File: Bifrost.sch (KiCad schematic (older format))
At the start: 55 parts, among them J1 OIP, U3 LMH6881, X1 SPXO-50M

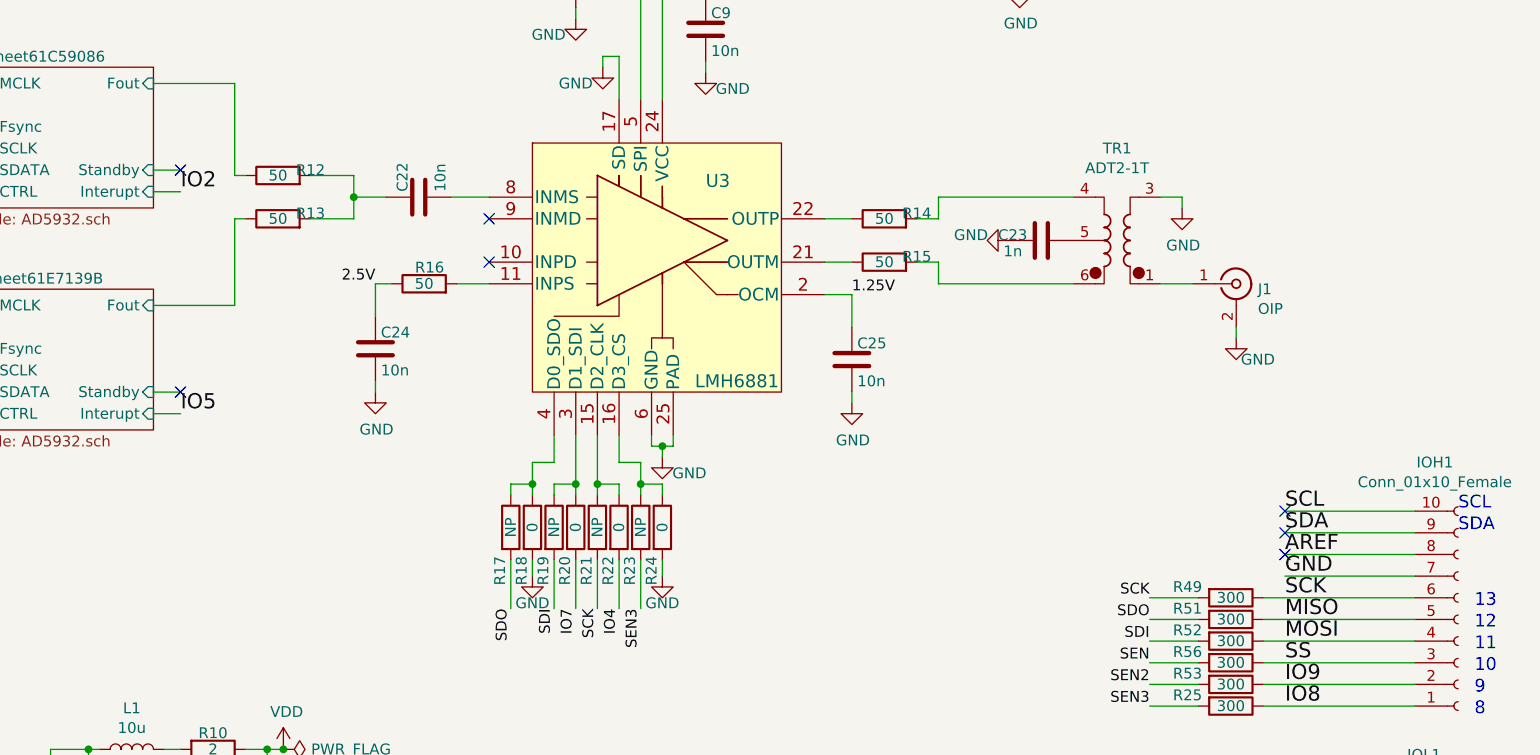
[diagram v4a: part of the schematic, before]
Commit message: put the AD5932's Standby to the ground
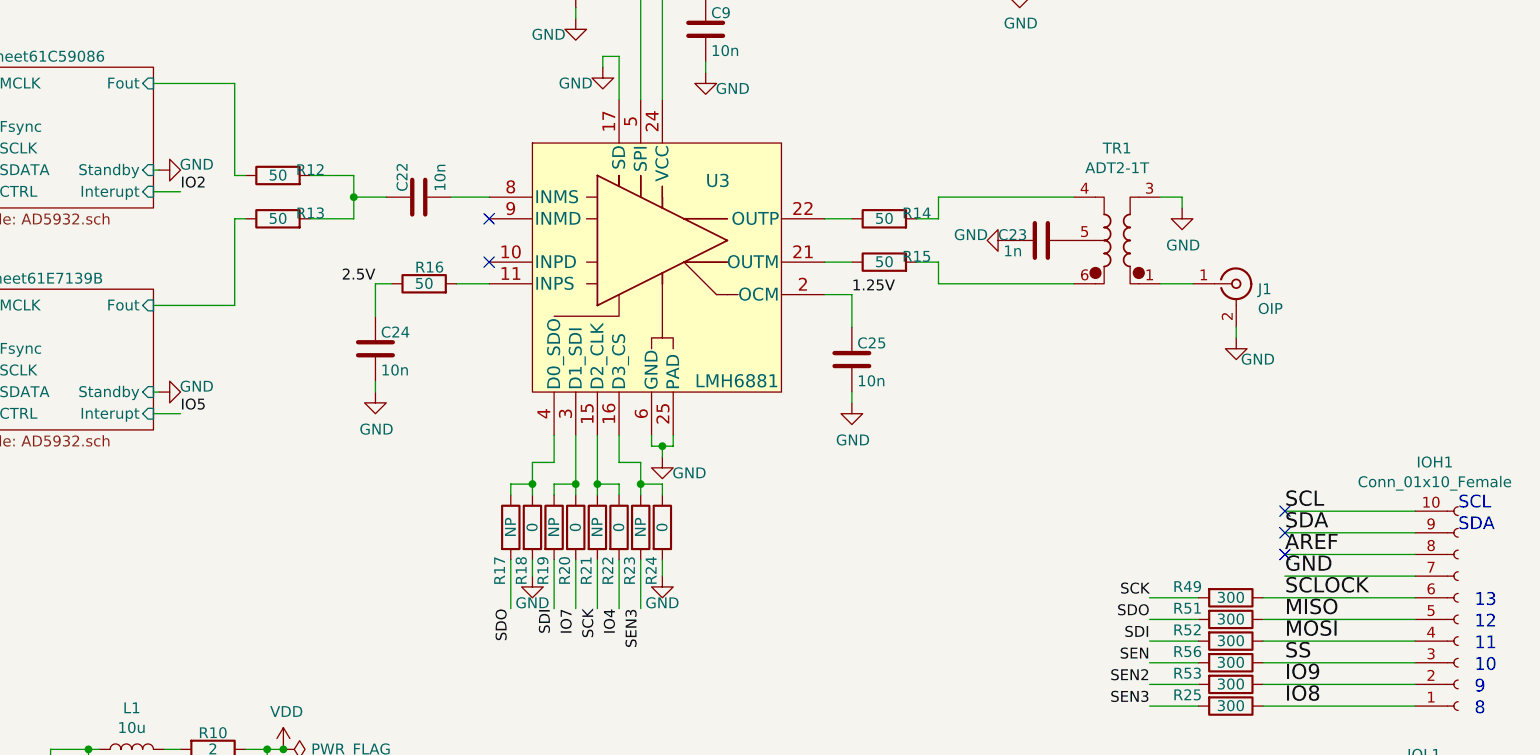
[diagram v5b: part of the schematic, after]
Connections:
- net SCK: no longer IOH1.6 (Pin_6), R49.1
- new net SCLOCK: IOH1.6 (Pin_6), R49.1
- no-connect marks 28 -> 26
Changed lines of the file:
@@
 GND
 Text Label 10000 4550 0    70   ~ 0
-SCK
+SCLOCK
 Text Label 10000 4650 0    70   ~ 0
 MISO
@@
 Text Label 3625 2675 2    70   ~ 0
 IO3
-Text Label 4900 2675 0    70   ~ 0
+Text Label 4900 2675 0    50   ~ 0
 IO2
 Wire Wire Line
@@
 	4775 2675 4900 2675
 Wire Wire Line
-	4775 2575 4900 2575
-Text Label 4900 3700 0    70   ~ 0
+	4775 2575 4800 2575
+Text Label 4900 3700 0    50   ~ 0
 IO5
 Text Label 3625 3700 2    70   ~ 0
@@
 	4775 3700 4900 3700
 Wire Wire Line
-	4775 3600 4900 3600
+	4775 3600 4800 3600
 Text Label 3625 3500 2    50   ~ 0
 SCK
@@
 Text Label 6725 4600 3    50   ~ 0
 IO7
-NoConn ~ 4900 3600
-NoConn ~ 4900 2575
 Wire Wire Line
 	6525 4375 6525 4450
@@
 Wire Wire Line
 	5200 6175 5300 6175
+$Comp
+L power:GND #PWR?
+U 1 1 6153F5AF
+P 4800 3600
+AR Path="/60D21B6E/6153F5AF" Ref="#PWR?"  Part="1"
+AR Path="/6153F5AF" Ref="#PWR?"  Part="1"
+F 0 "#PWR?" H 4800 3350 50  0001 C CNN
+F 1 "GND" V 4825 3425 50  0000 C CNN
+F 2 "" H 4800 3600 50  0001 C CNN
+F 3 "" H 4800 3600 50  0001 C CNN
+	1    4800 3600
+	0    -1   -1   0
+$EndComp
+$Comp
+L power:GND #PWR?
+U 1 1 6154B629
+P 4800 2575
+AR Path="/60D21B6E/6154B629" Ref="#PWR?"  Part="1"
+AR Path="/6154B629" Ref="#PWR?"  Part="1"
+F 0 "#PWR?" H 4800 2325 50  0001 C CNN
+F 1 "GND" V 4825 2400 50  0000 C CNN
+F 2 "" H 4800 2575 50  0001 C CNN
+F 3 "" H 4800 2575 50  0001 C CNN
+	1    4800 2575
+	0    -1   -1   0
+$EndComp
 $EndSCHEMATC

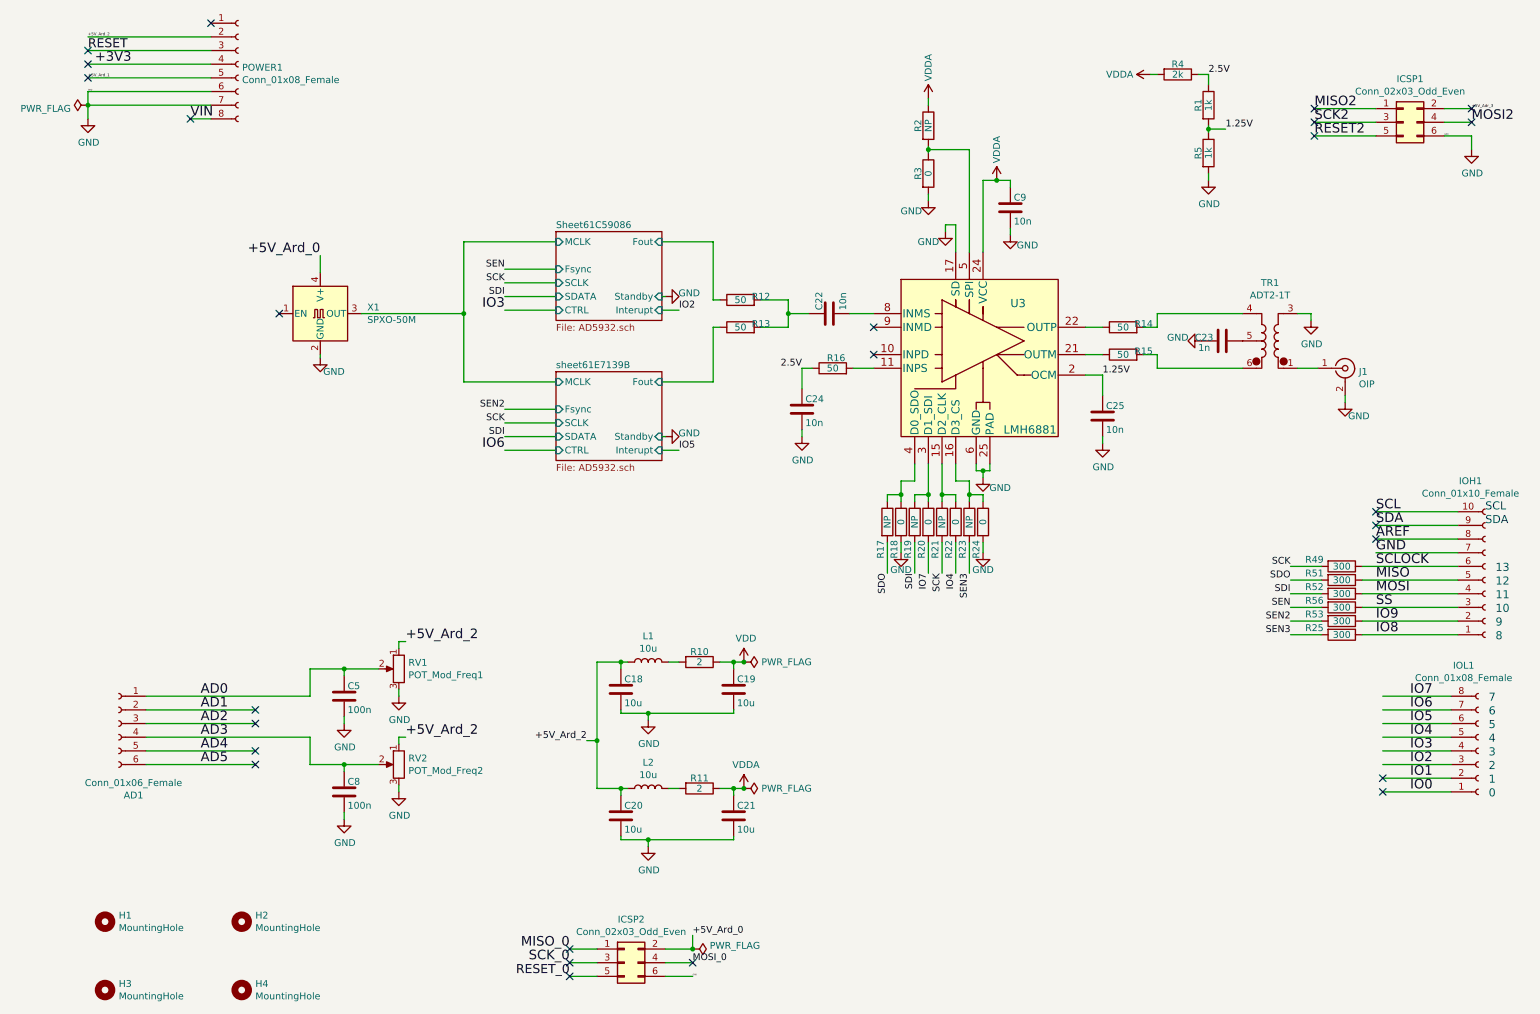
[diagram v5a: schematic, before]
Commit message: Changed gain pins for the LMH6881 and changed alim for the oscillator
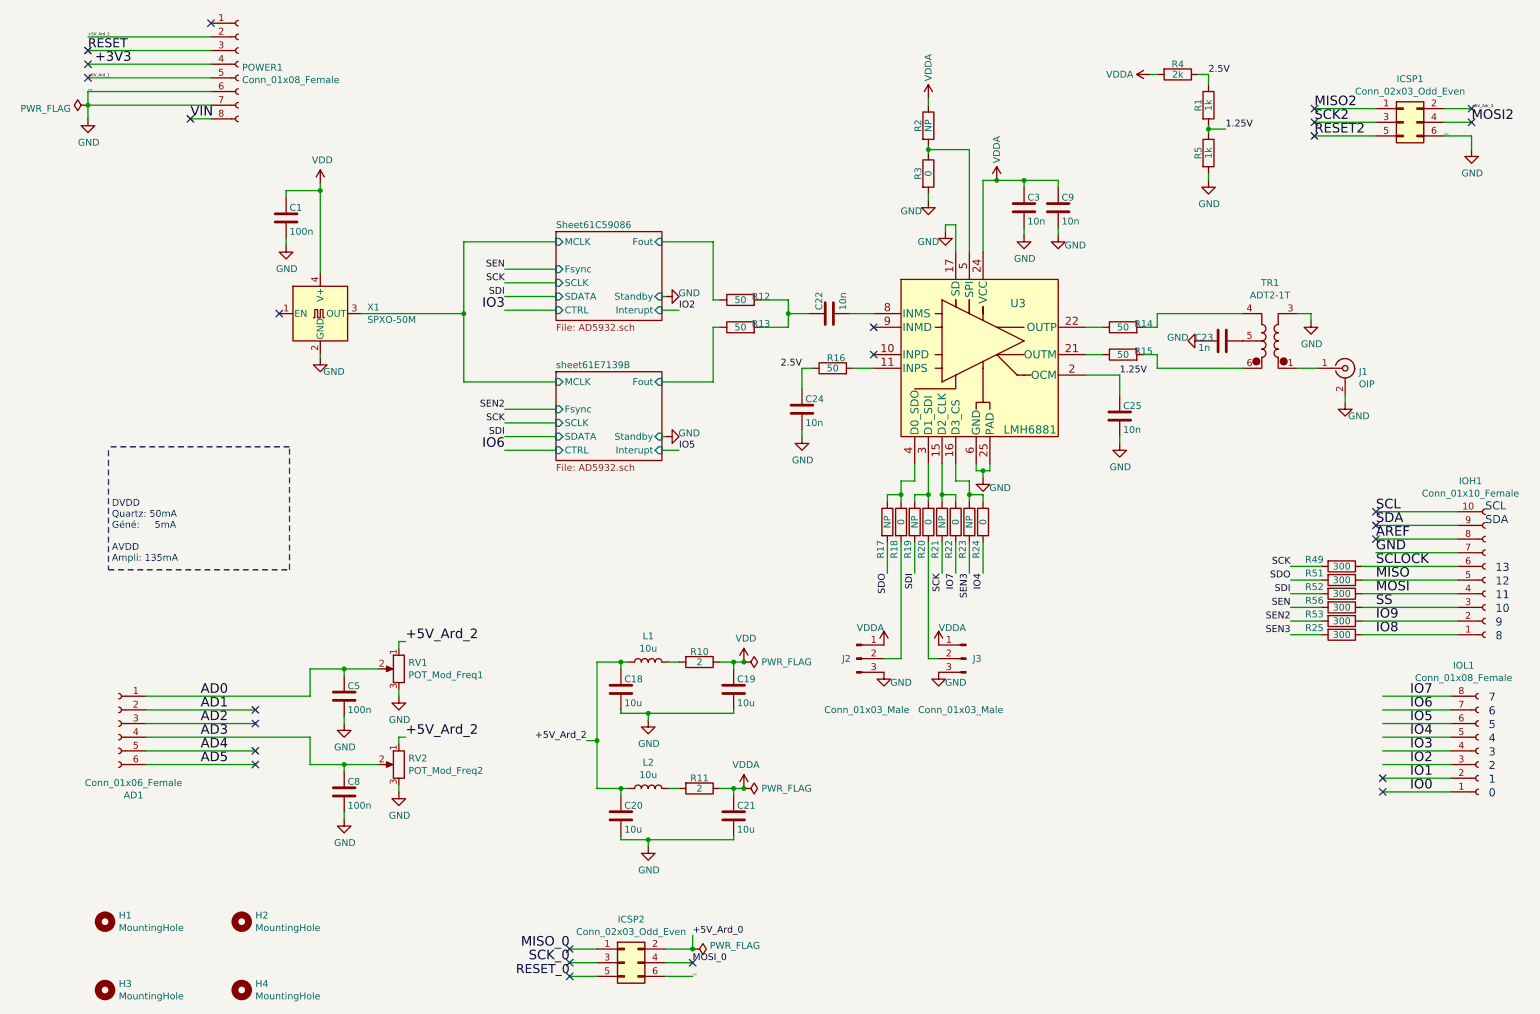
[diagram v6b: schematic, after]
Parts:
- added C1: 100n, Capacitor_SMD:C_0603_1608Metric_Pad1.08x0.95mm_HandSolder, symbol Device:C
- added C3: 10n, Capacitor_SMD:C_0603_1608Metric_Pad1.08x0.95mm_HandSolder, symbol Device:C
- added J2, J3: Conn_01x03_Male, Connector_PinHeader_2.54mm:PinHeader_1x03_P2.54mm_Vertical, symbol Connector:Conn_01x03_Male
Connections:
- net +5V_Ard_0: no longer X1.4 (V+)
- net GND: now also C1.1, C3.1, J2.3 (Pin_3), J3.3 (Pin_3); no longer R18.2, R24.2
- net IO4: now also R24.2; no longer R22.2
- net IO7: now also R22.2; no longer R20.2
- net VCC: now also C3.2, J2.1 (Pin_1), J3.1 (Pin_1)
- net VDD: now also X1.4 (V+), C1.2
- new net: J2.2 (Pin_2), R18.2
- new net: J3.2 (Pin_2), R20.2
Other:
- note added: "DVDD\nQuartz: 50mA\nGéné: 5mA\n\nAVDD\nAmpli: 135mA"
- moved on the sheet: C25, C9

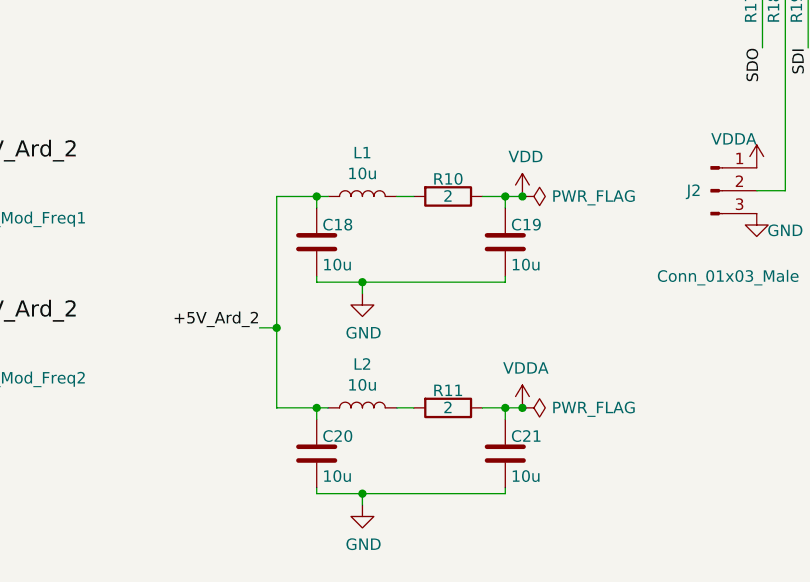
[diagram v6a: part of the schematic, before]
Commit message: Changed inductor and reststor on power filtration to limit DDP
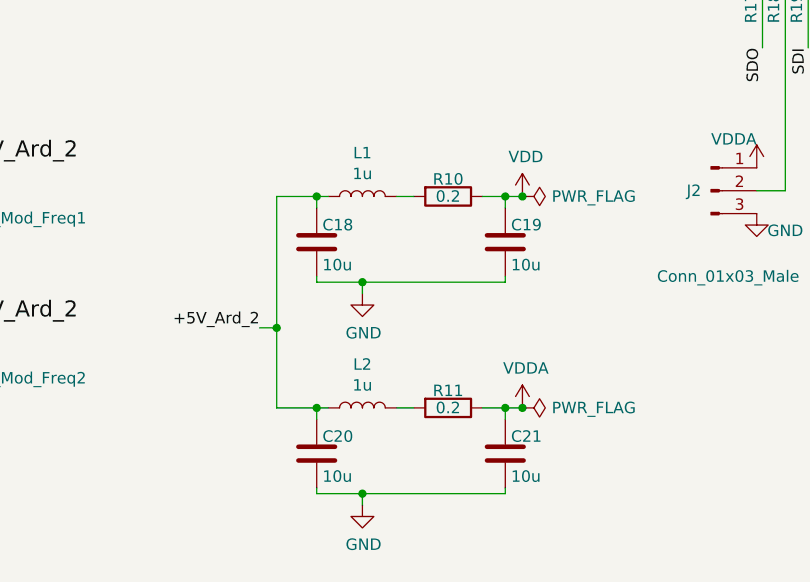
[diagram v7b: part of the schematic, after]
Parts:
- L1, L2: value 10u -> 1u
- R10, R11: value 2 -> 0.2
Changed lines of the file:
@@
 P 4675 5250
 F 0 "L1" V 4865 5250 50  0000 C CNN
-F 1 "10u" V 4774 5250 50  0000 C CNN
+F 1 "1u" V 4774 5250 50  0000 C CNN
 F 2 "Inductor_SMD:L_0603_1608Metric_Pad1.05x0.95mm_HandSolder" H 4675 5250 50  0001 C CNN
 F 3 "https://www.bourns.com/docs/product-datasheets/CWF1610.pdf" H 4675 5250 50  0001 C CNN
@@
 P 4675 6175
 F 0 "L2" V 4865 6175 50  0000 C CNN
-F 1 "10u" V 4774 6175 50  0000 C CNN
+F 1 "1u" V 4774 6175 50  0000 C CNN
 F 2 "Inductor_SMD:L_0603_1608Metric_Pad1.05x0.95mm_HandSolder" H 4675 6175 50  0001 C CNN
 F 3 "https://www.bourns.com/docs/product-datasheets/CWF1610.pdf" H 4675 6175 50  0001 C CNN
@@
 P 5050 5250
 F 0 "R10" V 4975 5250 50  0000 C CNN
-F 1 "2" V 5050 5250 50  0000 C CNN
+F 1 "0.2" V 5050 5250 50  0000 C CNN
 F 2 "Resistor_SMD:R_0603_1608Metric_Pad0.98x0.95mm_HandSolder" V 4980 5250 50  0001 C CNN
 F 3 "~" H 5050 5250 50  0001 C CNN
@@
 P 5050 6175
 F 0 "R11" V 4975 6175 50  0000 C CNN
-F 1 "2" V 5050 6175 50  0000 C CNN
+F 1 "0.2" V 5050 6175 50  0000 C CNN
 F 2 "Resistor_SMD:R_0603_1608Metric_Pad0.98x0.95mm_HandSolder" V 4980 6175 50  0001 C CNN
 F 3 "~" H 5050 6175 50  0001 C CNN

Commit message: Same as the last part 2
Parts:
- U3: footprint Package_DFN_QFN:WQFN-24-1EP_4x4mm_P0.5mm_EP2.45x2.45mm -> Package_DFN_QFN:WQFN-24-1EP_4x4mm_P0.5mm_EP2.45x2.45mm_ThermalVias
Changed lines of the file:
@@
 F 0 "U3" H 7325 3175 60  0000 L CNN
 F 1 "LMH6881" H 7275 2250 60  0000 L CNN
-F 2 "Package_DFN_QFN:WQFN-24-1EP_4x4mm_P0.5mm_EP2.45x2.45mm" H 7075 2840 60  0001 C CNN
+F 2 "Package_DFN_QFN:WQFN-24-1EP_4x4mm_P0.5mm_EP2.45x2.45mm_ThermalVias" H 7075 2840 60  0001 C CNN
 F 3 "https://www.ti.com/lit/ds/symlink/lmh6881.pdf" H 7919 2669 60  0001 L CNN
 	1    7125 2900
